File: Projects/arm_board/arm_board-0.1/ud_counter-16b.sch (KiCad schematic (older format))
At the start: 2 parts, among them U1 74HC4067, U6 MC14013B

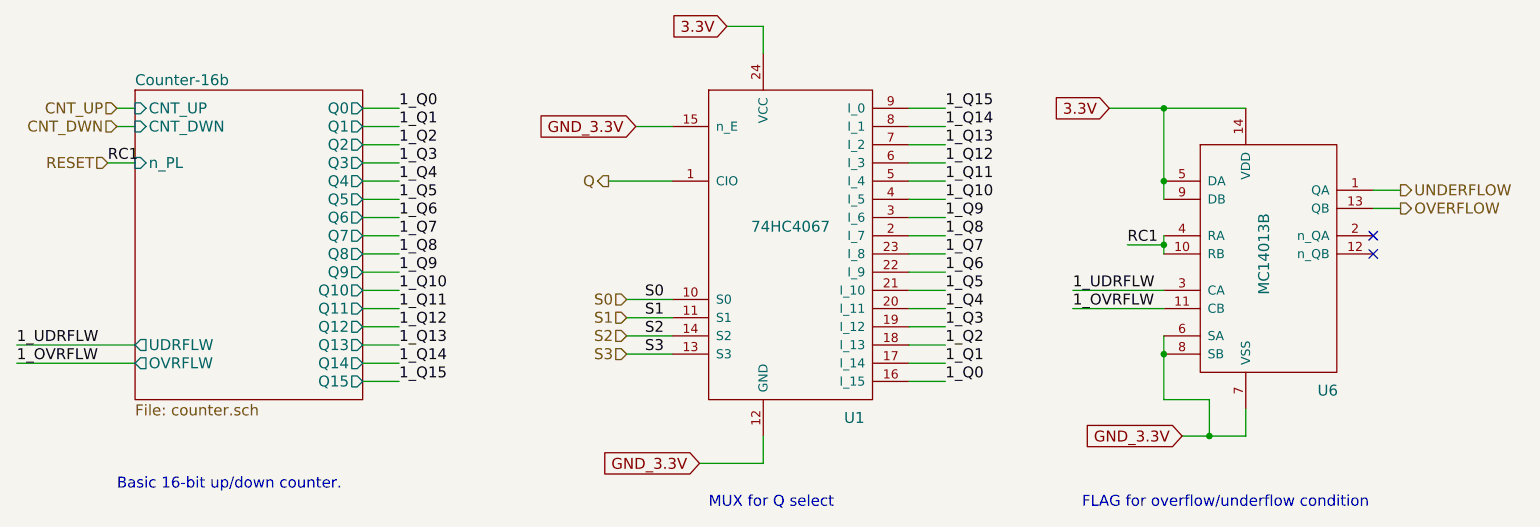
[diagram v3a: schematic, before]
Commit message: Arm Board: bug fixes, and added footprints
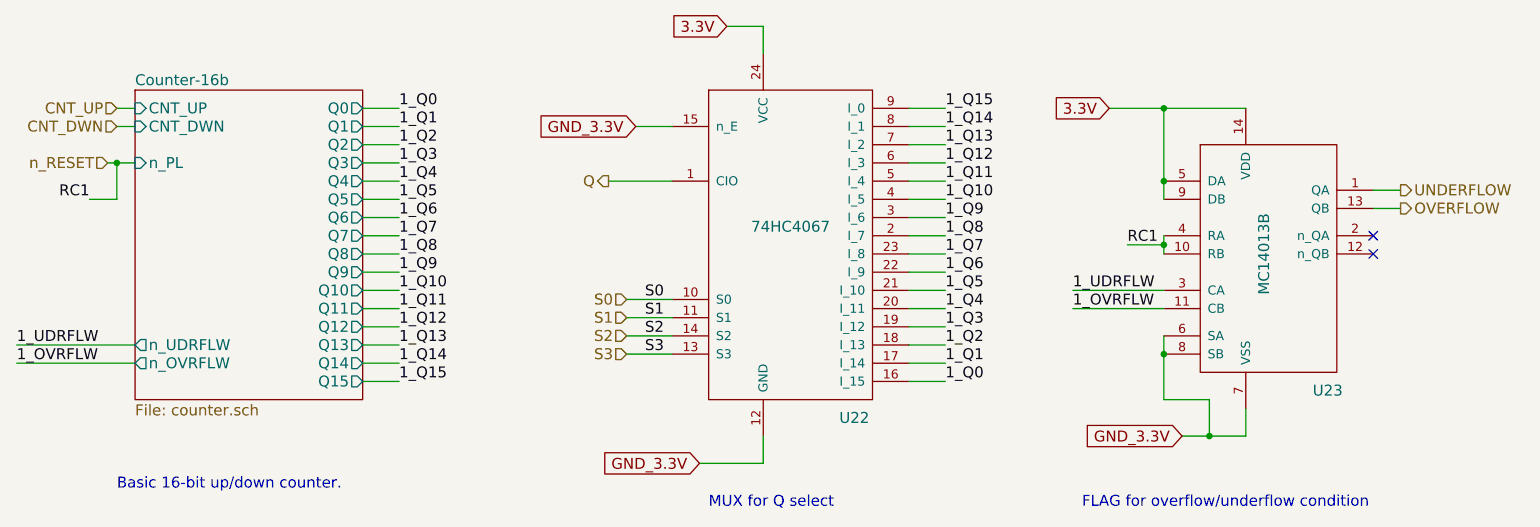
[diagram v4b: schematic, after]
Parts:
- U15: renamed from U1; footprint (none) -> SMD_Packages:SOIC-24
- U16: renamed from U6; footprint (none) -> SMD_Packages:SOIC-14_N
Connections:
- net RESET renamed n_RESET
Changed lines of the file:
@@
 LIBS:ArmComponentLibrary
 LIBS:arm_board-cache
-EELAYER 27 0
+EELAYER 25 0
 EELAYER END
 $Descr A4 11693 8268
 encoding utf-8
-Sheet 22 23
+Sheet 7 23
 Title ""
 Date "30 jan 2016"
@@
 $EndDescr
 $Comp
-L 74HC4067 U1
+L 74HC4067 U15
 U 1 1 564A929C
 P 5900 2800
-AR Path="/564B31DF/564A908F/564A929C" Ref="U1"  Part="1"
-AR Path="/56666F75/564A908F/564A929C" Ref="U1"  Part="1"
-AR Path="/56669634/564A908F/564A929C" Ref="U1"  Part="1"
-AR Path="/56669644/564A908F/564A929C" Ref="U1"  Part="1"
-AR Path="/5666D2E0/564A908F/564A929C" Ref="U1"  Part="1"
-AR Path="/5666D2F0/564A908F/564A929C" Ref="U1"  Part="1"
-AR Path="/56F53B7D/564A908F/564A929C" Ref="U1"  Part="1"
-AR Path="/56F75F1F/564A908F/564A929C" Ref="U1"  Part="1"
-F 0 "U1" H 6250 1800 60  0000 C CNN
+AR Path="/56F5245F/564A908F/564A929C" Ref="U15"  Part="1"
+AR Path="/56F53B7D/564A908F/564A929C" Ref="U22"  Part="1"
+AR Path="/56F544AF/564A908F/564A929C" Ref="U29"  Part="1"
+AR Path="/56F55E0D/564A908F/564A929C" Ref="U36"  Part="1"
+AR Path="/56F56B2F/564A908F/564A929C" Ref="U43"  Part="1"
+AR Path="/56F75F1F/56AED673/564A929C" Ref="U50"  Part="1"
+F 0 "U22" H 6250 1800 60  0000 C CNN
 F 1 "74HC4067" H 5900 2850 60  0000 C CNN
-F 2 "" H 5850 3150 60  0000 C CNN
+F 2 "SMD_Packages:SOIC-24" H 5850 3150 60  0001 C CNN
 F 3 "" H 5850 3150 60  0000 C CNN
 	1    5900 2800
@@
 F19 "Q14" O R 3550 3500 60
 F20 "Q15" O R 3550 3600 60
-F21 "UDRFLW" O L 2300 3400 60
-F22 "OVRFLW" O L 2300 3500 60
+F21 "n_UDRFLW" O L 2300 3400 60
+F22 "n_OVRFLW" O L 2300 3500 60
 $EndSheet
 Text GLabel 5050 2200 0    60   Input ~ 0
 GND_3.3V
 Text HLabel 2150 2400 0    60   Input ~ 0
-RESET
+n_RESET
 Wire Wire Line
 	3550 2800 3750 2800
@@
 	2150 2400 2300 2400
 $Comp
-L MC14013B U6
+L MC14013B U16
 U 1 1 5659B370
 P 8500 2900
-AR Path="/564B31DF/564A908F/5659B370" Ref="U6"  Part="1"
-AR Path="/56666F75/564A908F/5659B370" Ref="U6"  Part="1"
-AR Path="/56669634/564A908F/5659B370" Ref="U6"  Part="1"
-AR Path="/56669644/564A908F/5659B370" Ref="U6"  Part="1"
-AR Path="/5666D2E0/564A908F/5659B370" Ref="U6"  Part="1"
-AR Path="/5666D2F0/564A908F/5659B370" Ref="U6"  Part="1"
-AR Path="/56F53B7D/564A908F/5659B370" Ref="U6"  Part="1"
-AR Path="/56F75F1F/564A908F/5659B370" Ref="U6"  Part="1"
-F 0 "U6" H 8850 2150 60  0000 C CNN
+AR Path="/56F5245F/564A908F/5659B370" Ref="U16"  Part="1"
+AR Path="/56F53B7D/564A908F/5659B370" Ref="U23"  Part="1"
+AR Path="/56F544AF/564A908F/5659B370" Ref="U30"  Part="1"
+AR Path="/56F55E0D/564A908F/5659B370" Ref="U37"  Part="1"
+AR Path="/56F56B2F/564A908F/5659B370" Ref="U44"  Part="1"
+AR Path="/56F75F1F/56AED673/5659B370" Ref="U51"  Part="1"
+F 0 "U23" H 8850 2150 60  0000 C CNN
 F 1 "MC14013B" V 8500 2900 60  0000 C CNN
-F 2 "" V 8600 2900 60  0000 C CNN
+F 2 "SMD_Packages:SOIC-14_N" V 8600 2900 60  0001 C CNN
 F 3 "" V 8600 2900 60  0000 C CNN
 	1    8500 2900
@@
 Text Label 5100 3450 0    60   ~ 0
 S3
-Text Label 2150 2400 0    60   ~ 0
+Text Label 2050 2600 2    60   ~ 0
 RC1
 Text Label 7750 2850 0    60   ~ 0
@@
 Text Notes 7500 4300 0    60   ~ 0
 FLAG for overflow/underflow condition
+Wire Wire Line
+	2050 2600 2200 2600
+Wire Wire Line
+	2200 2600 2200 2400
+Connection ~ 2200 2400
 $EndSCHEMATC

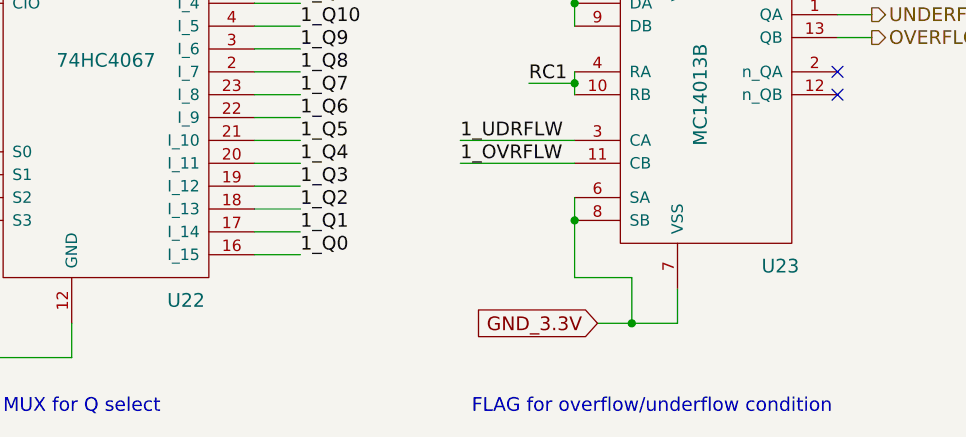
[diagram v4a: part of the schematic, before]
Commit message: Arm Board: bug fixes, cleanup, and start PCB layout
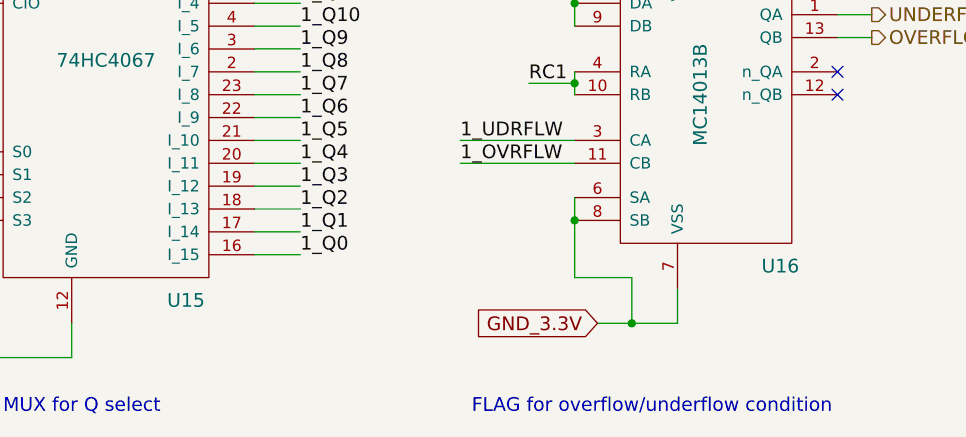
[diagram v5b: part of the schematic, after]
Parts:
- removed U16: MC14013B, SMD_Packages:SOIC-14_N, symbol MC14013B
- added U49: MC14013B, SMD_Packages:SOIC-14_N, symbol MC14013B
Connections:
- net 1_OVRFLW: now also U49.11 (CB)
- net 1_UDRFLW: now also U49.3 (CA)
- net 3.3V: now also U49.14 (VDD), U49.5 (DA), U49.9 (DB)
- net GND_3.3V: now also U49.6 (SA), U49.7 (VSS), U49.8 (SB)
- net OVERFLOW: now also U49.13 (QB)
- net UNDERFLOW: now also U49.1 (QA)
- net n_RESET: now also U49.10 (RB), U49.4 (RA)
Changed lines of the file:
@@
 $Descr A4 11693 8268
 encoding utf-8
-Sheet 7 23
+Sheet 19 23
 Title ""
 Date "30 jan 2016"
@@
 Comment4 ""
 $EndDescr
-$Comp
-L 74HC4067 U15
-U 1 1 564A929C
-P 5900 2800
-AR Path="/56F5245F/564A908F/564A929C" Ref="U15"  Part="1"
-AR Path="/56F53B7D/564A908F/564A929C" Ref="U22"  Part="1"
-AR Path="/56F544AF/564A908F/564A929C" Ref="U29"  Part="1"
-AR Path="/56F55E0D/564A908F/564A929C" Ref="U36"  Part="1"
-AR Path="/56F56B2F/564A908F/564A929C" Ref="U43"  Part="1"
-AR Path="/56F75F1F/56AED673/564A929C" Ref="U50"  Part="1"
-F 0 "U22" H 6250 1800 60  0000 C CNN
-F 1 "74HC4067" H 5900 2850 60  0000 C CNN
-F 2 "SMD_Packages:SOIC-24" H 5850 3150 60  0001 C CNN
-F 3 "" H 5850 3150 60  0000 C CNN
-	1    5900 2800
-	1    0    0    -1
-$EndComp
 Text Label 3750 2800 0    60   ~ 0
 1_Q7
@@
 Wire Wire Line
 	2150 2400 2300 2400
-$Comp
-L MC14013B U16
-U 1 1 5659B370
-P 8500 2900
-AR Path="/56F5245F/564A908F/5659B370" Ref="U16"  Part="1"
-AR Path="/56F53B7D/564A908F/5659B370" Ref="U23"  Part="1"
-AR Path="/56F544AF/564A908F/5659B370" Ref="U30"  Part="1"
-AR Path="/56F55E0D/564A908F/5659B370" Ref="U37"  Part="1"
-AR Path="/56F56B2F/564A908F/5659B370" Ref="U44"  Part="1"
-AR Path="/56F75F1F/56AED673/5659B370" Ref="U51"  Part="1"
-F 0 "U23" H 8850 2150 60  0000 C CNN
-F 1 "MC14013B" V 8500 2900 60  0000 C CNN
-F 2 "SMD_Packages:SOIC-14_N" V 8600 2900 60  0001 C CNN
-F 3 "" V 8600 2900 60  0000 C CNN
-	1    8500 2900
-	1    0    0    -1
-$EndComp
 Text GLabel 7650 2100 0    60   Input ~ 0
 3.3V
@@
 	2200 2600 2200 2400
 Connection ~ 2200 2400
+$Comp
+L MC14013B U49
+U 1 1 56C78081
+P 8500 2900
+AR Path="/56F75F1F/56AED673/56C78081" Ref="U49"  Part="1"
+AR Path="/56F5245F/564A908F/56C78081" Ref="U16"  Part="1"
+AR Path="/56F544AF/564A908F/56C78081" Ref="U23"  Part="1"
+AR Path="/56F55E0D/564A908F/56C78081" Ref="U30"  Part="1"
+AR Path="/56F56B2F/564A908F/56C78081" Ref="U37"  Part="1"
+AR Path="/56F53B7D/564A908F/56C78081" Ref="U51"  Part="1"
+F 0 "U16" H 8850 2150 60  0000 C CNN
+F 1 "MC14013B" V 8500 2900 60  0000 C CNN
+F 2 "SMD_Packages:SOIC-14_N" V 8600 2900 60  0001 C CNN
+F 3 "" V 8600 2900 60  0000 C CNN
+	1    8500 2900
+	1    0    0    -1
+$EndComp
+$Comp
+L 74HC4067 U15
+U 1 1 56CA6B36
+P 5900 2800
+AR Path="/56F5245F/564A908F/56CA6B36" Ref="U15"  Part="1"
+AR Path="/56F75F1F/56AED673/56CA6B36" Ref="U43"  Part="1"
+AR Path="/56F544AF/564A908F/56CA6B36" Ref="U22"  Part="1"
+AR Path="/56F55E0D/564A908F/56CA6B36" Ref="U29"  Part="1"
+AR Path="/56F56B2F/564A908F/56CA6B36" Ref="U36"  Part="1"
+AR Path="/56F53B7D/564A908F/56CA6B36" Ref="U50"  Part="1"
+F 0 "U15" H 6250 1800 60  0000 C CNN
+F 1 "74HC4067" H 5900 2850 60  0000 C CNN
+F 2 "SMD_Packages:SOIC-24" H 5850 3150 60  0001 C CNN
+F 3 "" H 5850 3150 60  0000 C CNN
+	1    5900 2800
+	1    0    0    -1
+$EndComp
 $EndSCHEMATC

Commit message: Arm Board: finalizing footprints.
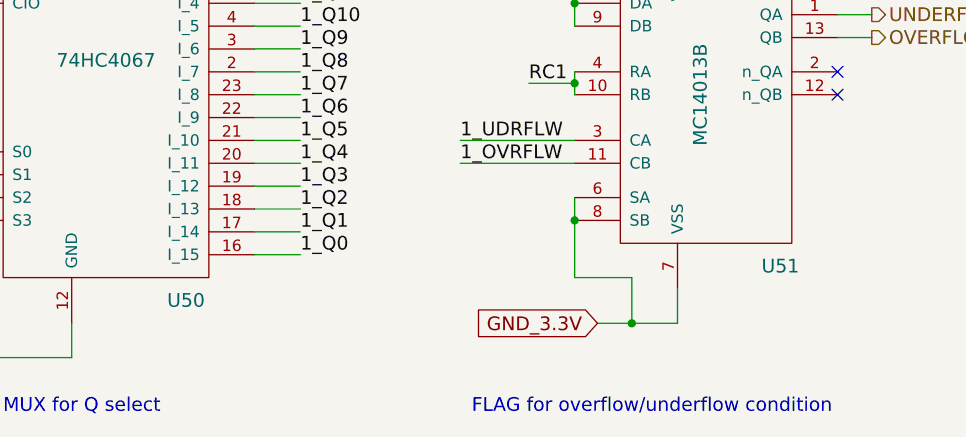
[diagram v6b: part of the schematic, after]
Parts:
- U15: footprint SMD_Packages:SOIC-24 -> ArmFootprints:SOIC-24
- U49: footprint SMD_Packages:SOIC-14_N -> ArmFootprints:SOIC-14
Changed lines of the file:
@@
 AR Path="/56F56B2F/564A908F/56C78081" Ref="U37"  Part="1"
 AR Path="/56F53B7D/564A908F/56C78081" Ref="U51"  Part="1"
-F 0 "U16" H 8850 2150 60  0000 C CNN
+F 0 "U51" H 8850 2150 60  0000 C CNN
 F 1 "MC14013B" V 8500 2900 60  0000 C CNN
-F 2 "SMD_Packages:SOIC-14_N" V 8600 2900 60  0001 C CNN
+F 2 "ArmFootprints:SOIC-14" V 8600 2900 60  0001 C CNN
 F 3 "" V 8600 2900 60  0000 C CNN
 	1    8500 2900
@@
 AR Path="/56F56B2F/564A908F/56CA6B36" Ref="U36"  Part="1"
 AR Path="/56F53B7D/564A908F/56CA6B36" Ref="U50"  Part="1"
-F 0 "U15" H 6250 1800 60  0000 C CNN
+F 0 "U50" H 6250 1800 60  0000 C CNN
 F 1 "74HC4067" H 5900 2850 60  0000 C CNN
-F 2 "SMD_Packages:SOIC-24" H 5850 3150 60  0001 C CNN
+F 2 "ArmFootprints:SOIC-24" H 5850 3150 60  0001 C CNN
 F 3 "" H 5850 3150 60  0000 C CNN
 	1    5900 2800
